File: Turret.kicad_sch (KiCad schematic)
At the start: 19 parts, among them J1 Conn_01x04_Pin, J10 Conn_01x04_Pin, J11 Sabre Vertical Header 6, J12 Conn_01x02_Pin, J2 Conn_01x02_Pin, J20 Conn_01x02_Pin, J21 Conn_01x02_Pin, J3 Conn_01x02_Pin, J4 Conn_01x02_Pin, J5 Conn_01x04_Pin, J6 Conn_01x02_Pin, J7 Conn_01x02_Pin, J8 Conn_01x02_Pin, J9 Conn_01x02_Pin

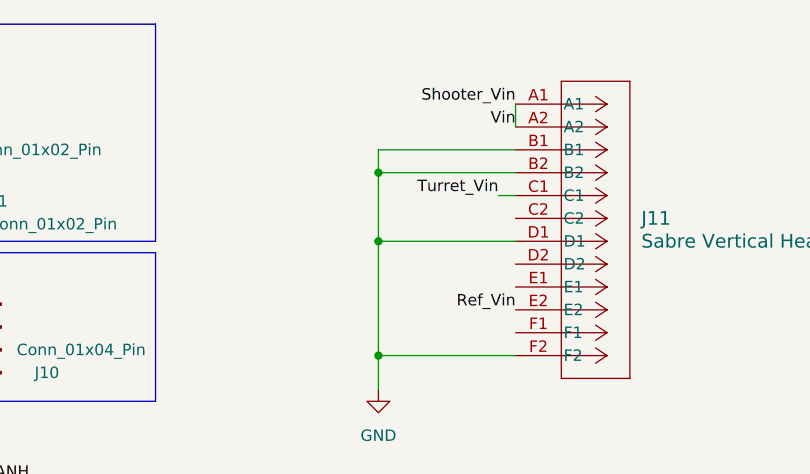
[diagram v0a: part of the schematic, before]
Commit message: Fixed 24V on sabre connector
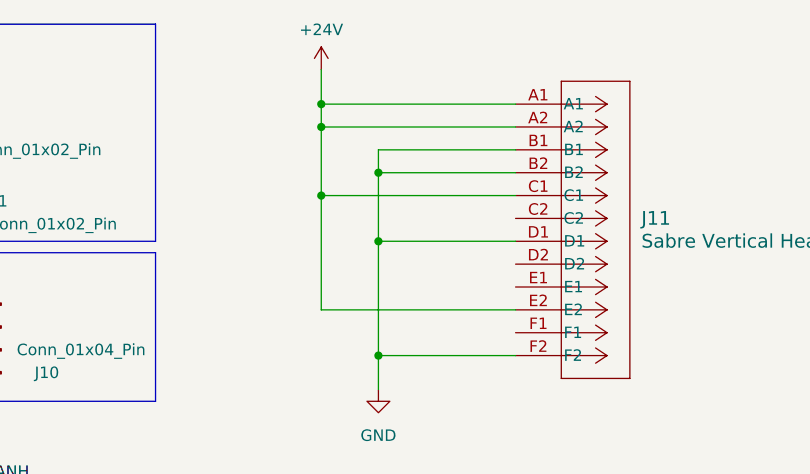
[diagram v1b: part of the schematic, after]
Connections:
- net Shooter_Vin is gone; now on net +24V: J11.A1, J11.A2
- net Turret_Vin is gone; now on net +24V: J11.C1
- net +24V: now also J11.E2
- net Ref_Vin: no longer J11.E2
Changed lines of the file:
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@@
 (kicad_sch (version 20230121) (generator eeschema)
   (paper "A4")
+  (junction (at 161.29 36.195) (diameter 0) (color 0 0 0 0)
+  )
   (junction (at 167.64 64.135) (diameter 0) (color 0 0 0 0)
   )
@@
   (junction (at 167.64 43.815) (diameter 0) (color 0 0 0 0)
   )
+  (junction (at 161.29 38.735) (diameter 0) (color 0 0 0 0)
+  )
+  (junction (at 161.29 46.355) (diameter 0) (color 0 0 0 0)
+  )
   (wire (pts (xy 28.575 46.355) (xy 30.48 46.355))
     (stroke (width 0) (type default))
@@
     (stroke (width 0) (type default))
   )
-  (wire (pts (xy 182.88 36.195) (xy 182.88 38.735))
+  (wire (pts (xy 182.88 36.195) (xy 161.29 36.195))
     (stroke (width 0) (type default))
   )
@@
     (stroke (width 0) (type default))
   )
+  (wire (pts (xy 161.29 36.195) (xy 161.29 38.735))
+    (stroke (width 0) (type default))
+  )
   (wire (pts (xy 38.735 81.28) (xy 36.195 81.28))
     (stroke (width 0) (type default))
@@
     (stroke (width 0) (type default))
   )
+  (wire (pts (xy 161.29 32.385) (xy 161.29 36.195))
+    (stroke (width 0) (type default))
+  )
   (wire (pts (xy 167.64 64.135) (xy 167.64 51.435))
     (stroke (width 0) (type default))
@@
     (stroke (width 0) (type default))
   )
-  (wire (pts (xy 180.975 46.355) (xy 182.88 46.355))
+  (wire (pts (xy 161.29 46.355) (xy 182.88 46.355))
     (stroke (width 0) (type default))
   )
@@
     (stroke (width 0) (type default))
   )
+  (wire (pts (xy 161.29 38.735) (xy 161.29 46.355))
+    (stroke (width 0) (type default))
+  )
   (wire (pts (xy 123.825 78.105) (xy 118.745 78.105))
     (stroke (width 0) (type default))
   )
+  (wire (pts (xy 182.88 59.055) (xy 161.29 59.055))
+    (stroke (width 0) (type default))
+  )
+  (wire (pts (xy 182.88 38.735) (xy 161.29 38.735))
+    (stroke (width 0) (type default))
+  )
   (wire (pts (xy 167.64 67.945) (xy 167.64 64.135))
     (stroke (width 0) (type default))
@@
     (stroke (width 0) (type default))
   )
+  (wire (pts (xy 161.29 59.055) (xy 161.29 46.355))
+    (stroke (width 0) (type default))
+  )
   (wire (pts (xy 26.67 40.005) (xy 26.67 41.275))
     (stroke (width 0) (type default))
@@
     (effects (font (size 1.27 1.27)) (justify left bottom))
   )
-  (label "Turret_Vin" (at 180.975 46.355 180) (fields_autoplaced)
-    (effects (font (size 1.27 1.27)) (justify right bottom))
-  )
   (label "Shooter_CANL" (at 78.74 45.085 180) (fields_autoplaced)
     (effects (font (size 1.27 1.27)) (justify right bottom))
@@
     (effects (font (size 1.27 1.27)) (justify right bottom))
   )
-  (label "Shooter_Vin" (at 182.88 36.195 180) (fields_autoplaced)
-    (effects (font (size 1.27 1.27)) (justify right bottom))
-  )
   (label "Turret_CANH" (at 117.475 46.99 180) (fields_autoplaced)
     (effects (font (size 1.27 1.27)) (justify right bottom))
@@
     (effects (font (size 1.27 1.27)) (justify right bottom))
   )
-  (label "Ref_Vin" (at 182.88 59.055 180) (fields_autoplaced)
-    (effects (font (size 1.27 1.27)) (justify right bottom))
-  )
   (label "UART_RX" (at 36.195 76.2 180) (fields_autoplaced)
     (effects (font (size 1.27 1.27)) (justify right bottom))
   )
   (label "Shooter_CANH" (at 78.74 61.595 180) (fields_autoplaced)
-    (effects (font (size 1.27 1.27)) (justify right bottom))
-  )
-  (label "Vin" (at 182.88 38.735 180) (fields_autoplaced)
     (effects (font (size 1.27 1.27)) (justify right bottom))
   )
@@
         )
       )
+    )
+  )
+  (symbol (lib_id "power:+24V") (at 161.29 32.385 0) (unit 1)
+    (in_bom yes) (on_board yes) (dnp no) (fields_autoplaced)
+    (property "Reference" "#PWR06" (at 161.29 36.195 0)
+      (effects (font (size 1.27 1.27)) hide)
+    )
+    (property "Value" "+24V" (at 161.29 27.94 0)
+      (effects (font (size 1.27 1.27)))
+    )
+    (property "Footprint" "" (at 161.29 32.385 0)
+      (effects (font (size 1.27 1.27)) hide)
+    )
+    (property "Datasheet" "" (at 161.29 32.385 0)
+      (effects (font (size 1.27 1.27)) hide)
+    )
+    (pin "1")
+    (instances
+      (project "Turret"
+        (path "/84905b3c-2997-4e61-b373-c0062fb72371"
+          (reference "#PWR06") (unit 1)
+        )
+      )

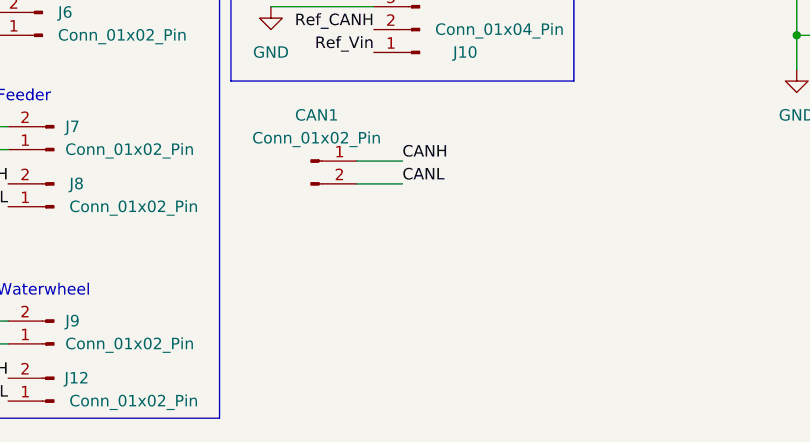
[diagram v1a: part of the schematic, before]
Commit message: turret dimensions
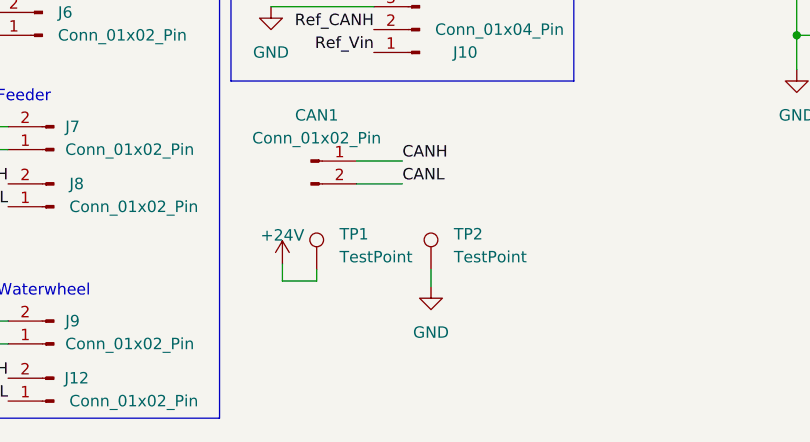
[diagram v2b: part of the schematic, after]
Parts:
- added TP1, TP2: TestPoint, TestPoint:TestPoint_Loop_D1.80mm_Drill1.0mm_Beaded, symbol Connector:TestPoint
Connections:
- net +24V: now also TP1.1
- net GND: now also TP2.1
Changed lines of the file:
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@@
+    (stroke (width 0) (type default))
+  )
+  (wire (pts (xy 127 90.17) (xy 127 92.075))
     (stroke (width 0) (type default))
   )
@@
     (stroke (width 0) (type default))
   )
+  (wire (pts (xy 110.49 91.44) (xy 114.3 91.44))
+    (stroke (width 0) (type default))
+  )
   (wire (pts (xy 70.485 95.885) (xy 80.01 95.885))
     (stroke (width 0) (type default))
@@
     (stroke (width 0) (type default))
   )
+  (wire (pts (xy 114.3 91.44) (xy 114.3 90.17))
+    (stroke (width 0) (type default))
+  )
   (wire (pts (xy 167.64 67.945) (xy 167.64 64.135))
     (stroke (width 0) (type default))
@@
   )
   (wire (pts (xy 26.67 40.005) (xy 26.67 41.275))
+    (stroke (width 0) (type default))
+  )
+  (wire (pts (xy 110.49 89.535) (xy 110.49 91.44))
     (stroke (width 0) (type default))
   )
@@
     )
   )
+  (symbol (lib_id "power:+24V") (at 110.49 89.535 0) (unit 1)
+    (in_bom yes) (on_board yes) (dnp no) (fields_autoplaced)
+    (property "Reference" "#PWR07" (at 110.49 93.345 0)
+      (effects (font (size 1.27 1.27)) hide)
+    )
+    (property "Value" "+24V" (at 110.49 86.36 0)
+      (effects (font (size 1.27 1.27)))
+    )
+    (property "Footprint" "" (at 110.49 89.535 0)
+      (effects (font (size 1.27 1.27)) hide)
+    )
+    (property "Datasheet" "" (at 110.49 89.535 0)
+      (effects (font (size 1.27 1.27)) hide)
+    )
+    (pin "1")
+    (instances
+      (project "Turret"
+        (path "/84905b3c-2997-4e61-b373-c0062fb72371"
+          (reference "#PWR07") (unit 1)
+        )
+      )
+    )
+  )
+  (symbol (lib_id "Connector:TestPoint") (at 127 90.17 0) (unit 1)
+    (in_bom yes) (on_board yes) (dnp no) (fields_autoplaced)
+    (property "Reference" "TP2" (at 129.54 86.233 0)
+      (effects (font (size 1.27 1.27)) (justify left))
+    )
+    (property "Value" "TestPoint" (at 129.54 88.773 0)
+      (effects (font (size 1.27 1.27)) (justify left))
+    )
+    (property "Footprint" "TestPoint:TestPoint_Loop_D1.80mm_Drill1.0mm_Beaded" (at 132.08 90.17 0)
+      (effects (font (size 1.27 1.27)) hide)
+    )
+    (property "Datasheet" "~" (at 132.08 90.17 0)
+      (effects (font (size 1.27 1.27)) hide)
+    )
+    (pin "1")
+    (instances
+      (project "Turret"
+        (path "/84905b3c-2997-4e61-b373-c0062fb72371"
+          (reference "TP2") (unit 1)
+        )
+      )
+    )
+  )
   (symbol (lib_id "power:GND") (at 109.22 60.96 0) (unit 1)
     (in_bom yes) (on_board yes) (dnp no) (fields_autoplaced)
@@
     )
   )
+  (symbol (lib_id "Connector:TestPoint") (at 114.3 90.17 0) (unit 1)
+    (in_bom yes) (on_board yes) (dnp no) (fields_autoplaced)
+    (property "Reference" "TP1" (at 116.84 86.233 0)
+      (effects (font (size 1.27 1.27)) (justify left))
+    )
+    (property "Value" "TestPoint" (at 116.84 88.773 0)
+      (effects (font (size 1.27 1.27)) (justify left))
+    )
+    (property "Footprint" "TestPoint:TestPoint_Loop_D1.80mm_Drill1.0mm_Beaded" (at 119.38 90.17 0)
+      (effects (font (size 1.27 1.27)) hide)
+    )
+    (property "Datasheet" "~" (at 119.38 90.17 0)
+      (effects (font (size 1.27 1.27)) hide)
+    )
+    (pin "1")
+    (instances
+      (project "Turret"
+        (path "/84905b3c-2997-4e61-b373-c0062fb72371"
+          (reference "TP1") (unit 1)
+        )
+      )
+    )
+  )
   (symbol (lib_id "Mechanical:MountingHole") (at 43.815 103.505 0) (unit 1)
     (in_bom yes) (on_board yes) (dnp no) (fields_autoplaced)
@@
         )
       )
+    )
+  )
+  (symbol (lib_id "power:GND") (at 127 92.075 0) (unit 1)
+    (in_bom yes) (on_board yes) (dnp no) (fields_autoplaced)
+    (property "Reference" "#PWR09" (at 127 98.425 0)
+      (effects (font (size 1.27 1.27)) hide)
+    )
+    (property "Value" "GND" (at 127 97.155 0)
+      (effects (font (size 1.27 1.27)))
+    )
+    (property "Footprint" "" (at 127 92.075 0)
+      (effects (font (size 1.27 1.27)) hide)
+    )
+    (property "Datasheet" "" (at 127 92.075 0)
+      (effects (font (size 1.27 1.27)) hide)
+    )
+    (pin "1")
+    (instances
+      (project "Turret"
+        (path "/84905b3c-2997-4e61-b373-c0062fb72371"
+          (reference "#PWR09") (unit 1)
+        )
+      )

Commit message: Turret change :)
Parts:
- added J13, J14: Conn_01x04_Pin, Connector_JST:JST_GH_BM04B-GHS-TBT_1x04-1MP_P1.25mm_Vertical, symbol Connector:Conn_01x04_Pin
- J1, J5: footprint (none) -> Connector_JST:JST_GH_BM04B-GHS-TBT_1x04-1MP_P1.25mm_Vertical
- J10: footprint Robomasters:866319112100004 -> ICs:866319112100004
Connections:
- net +3.3V: now also J13.4 (Pin_4), J14.4 (Pin_4)
- net GND: now also J13.1 (Pin_1), J14.1 (Pin_1)
- net SWCLK: now also J14.3 (Pin_3)
- net SWDIO: now also J14.2 (Pin_2)
- net UART_RX: now also J13.3 (Pin_3)
- net UART_TX: now also J13.2 (Pin_2)
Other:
- note added: "Remote Debug Connector PCB -> Devboard"
- note added: "Remote Debug Connector PCB -> Orin"
- note added: "UART Connection PCB -> Devboard"
- note added: "UART Connection PCB -> Orin"
- note removed: "Remote Debug Connector Orin -> Devboard"
- note removed: "UART Connection Orin -> Devboard"

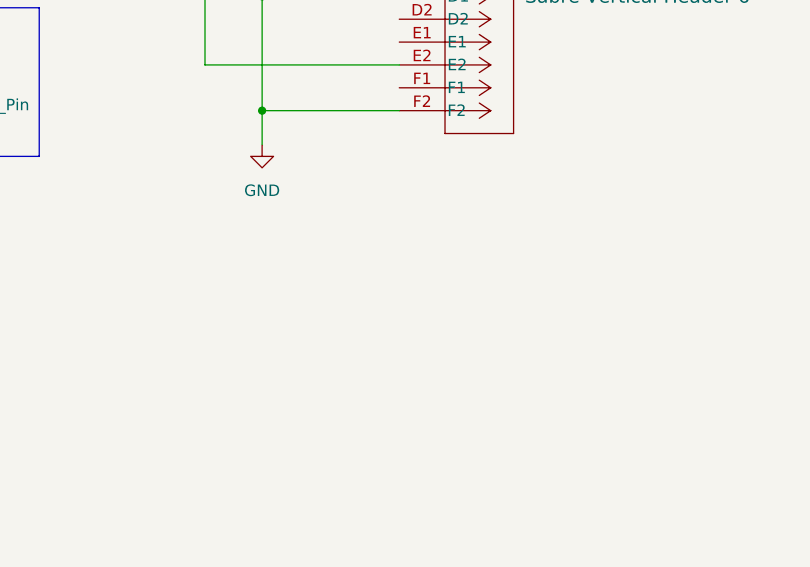
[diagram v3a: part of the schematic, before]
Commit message: Added 8 pin connector, 1-4 gnd and 5-8 +24V
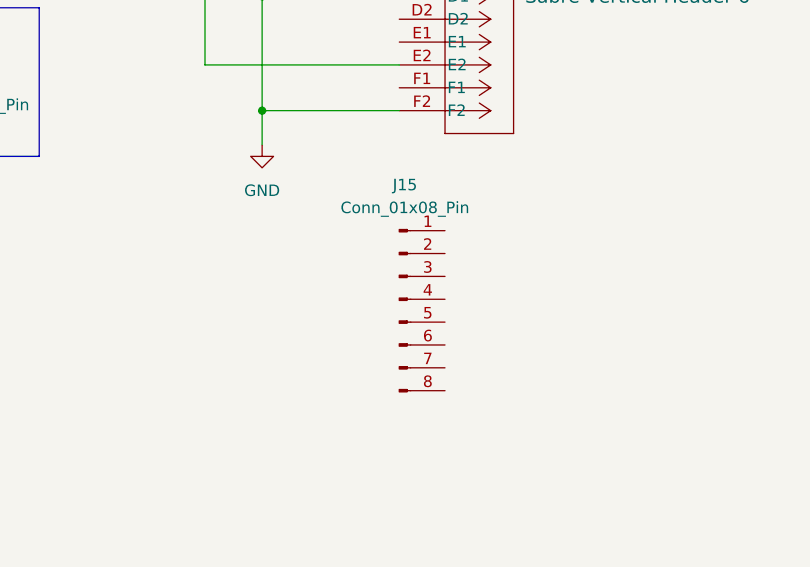
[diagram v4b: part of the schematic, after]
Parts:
- added J15: Conn_01x08_Pin, symbol Connector:Conn_01x08_Pin
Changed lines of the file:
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@@
+    )
+  )
+  (symbol (lib_id "Connector:Conn_01x08_Pin") (at 182.88 85.09 0) (unit 1)
+    (in_bom yes) (on_board yes) (dnp no) (fields_autoplaced)
+    (property "Reference" "J15" (at 183.515 72.39 0)
+      (effects (font (size 1.27 1.27)))
+    )
+    (property "Value" "Conn_01x08_Pin" (at 183.515 74.93 0)
+      (effects (font (size 1.27 1.27)))
+    )
+    (property "Footprint" "" (at 182.88 85.09 0)
+      (effects (font (size 1.27 1.27)) hide)
+    )
+    (property "Datasheet" "~" (at 182.88 85.09 0)
+      (effects (font (size 1.27 1.27)) hide)
+    )
+    (pin "1")
+    (pin "2")
+    (pin "3")
+    (pin "4")
+    (pin "5")
+    (pin "6")
+    (pin "7")
+    (pin "8")
+    (instances
+      (project "Turret"
+        (path "/84905b3c-2997-4e61-b373-c0062fb72371"
+          (reference "J15") (unit 1)
+        )
+      )
     )
   )
